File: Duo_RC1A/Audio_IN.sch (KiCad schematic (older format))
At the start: 120 parts, among them J1 JACK_P10_TRS_6P, J2 JACK_P10_TRS_6P

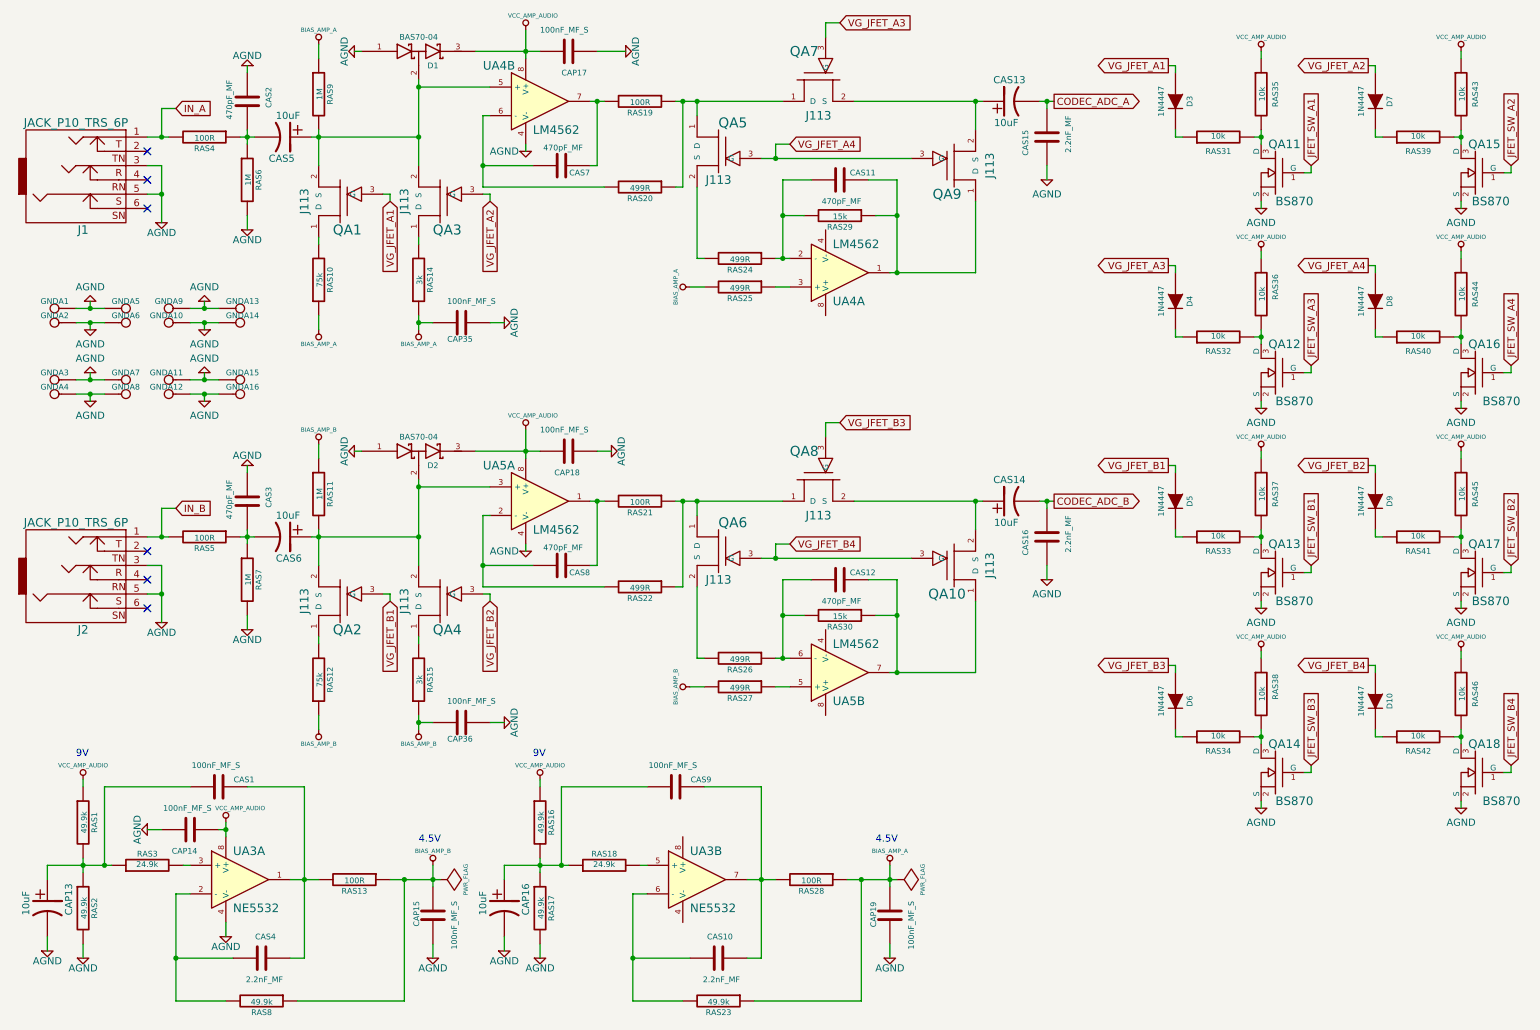
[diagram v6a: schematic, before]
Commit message: Eliminated extra signals from the audio codec (MVP). Saving before moving the audio bias circuit module.
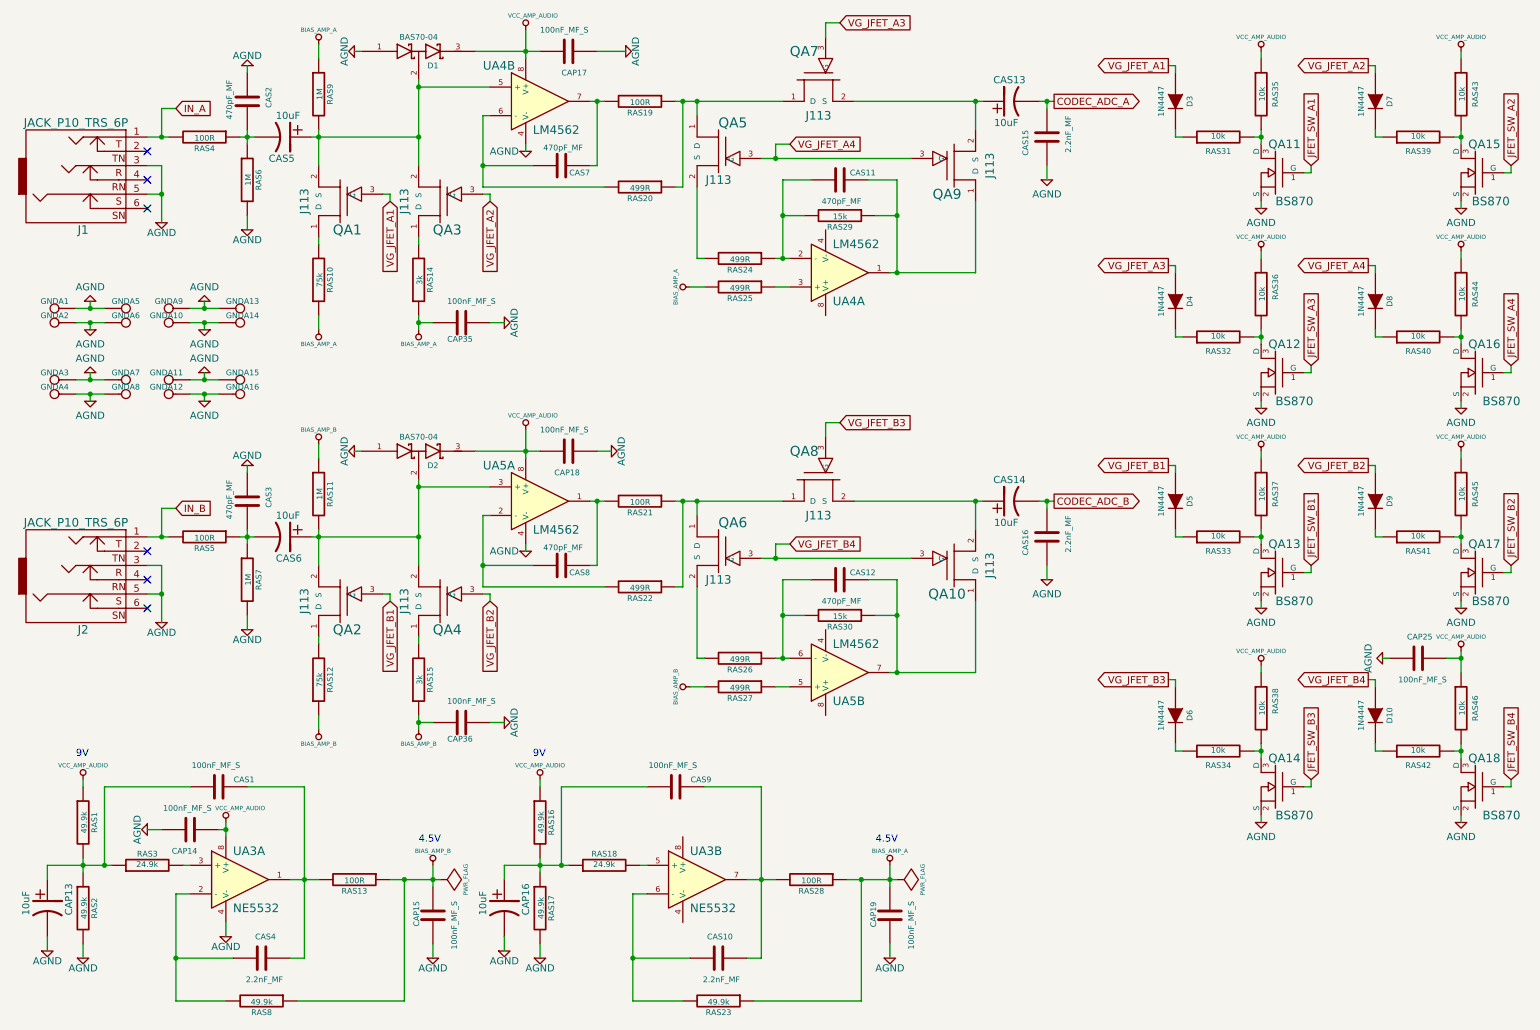
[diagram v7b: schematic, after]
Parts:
- added CAP25: 100nF_MF_S, Duo_Audio_HMI_RC1A:CapacitorMetalFilm_7.2x2.5MM_P5MM, symbol C
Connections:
- net AGND: now also CAP25.1
- net VCC_AMP_AUDIO: now also CAP25.2
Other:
- moved on the sheet: D10, D6, QA14, QA18, RAS34, RAS38, RAS42, RAS46
